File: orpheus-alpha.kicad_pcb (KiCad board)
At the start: 2 copper layers, 84.8 x 54.4 mm, 60 parts, among them J1 Signal in, J2 AC in, J3 Signal out, J4 uC

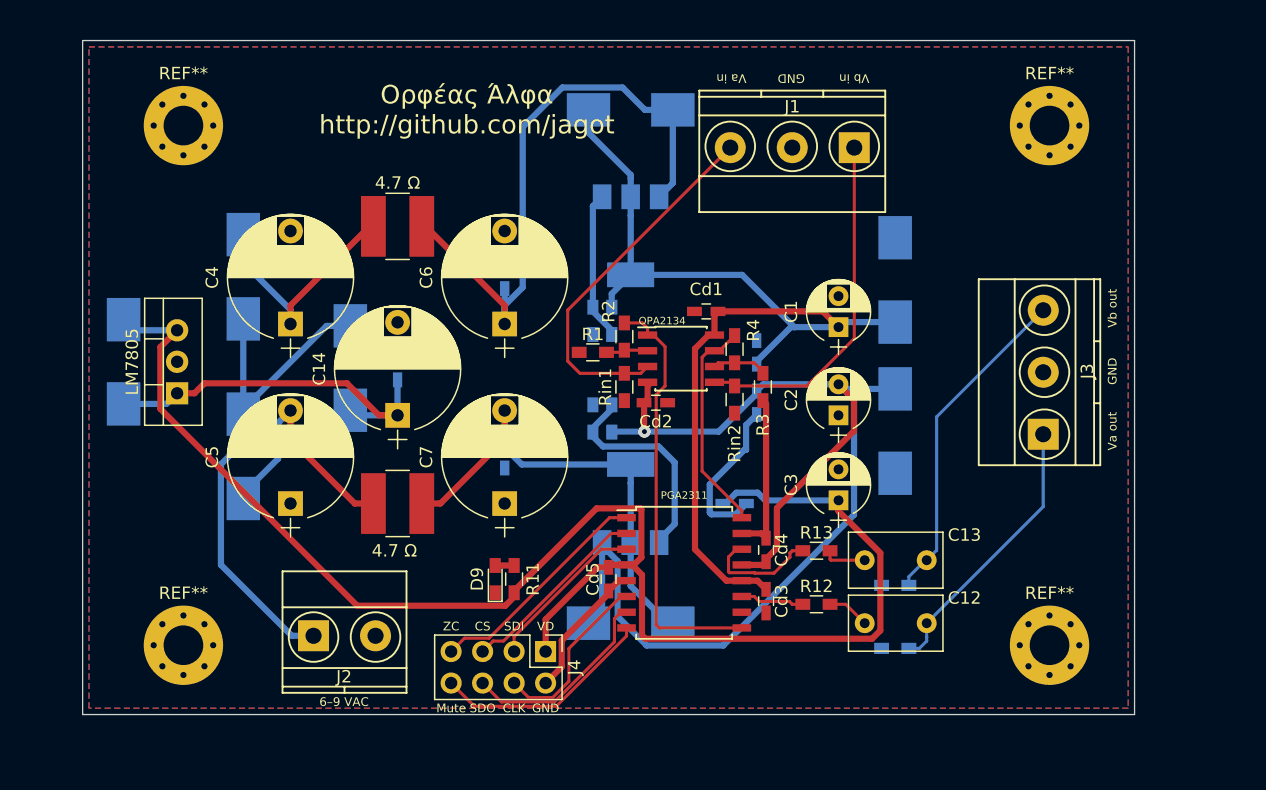
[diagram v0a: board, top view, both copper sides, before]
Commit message: Small changes, changed output coupling caps to film type
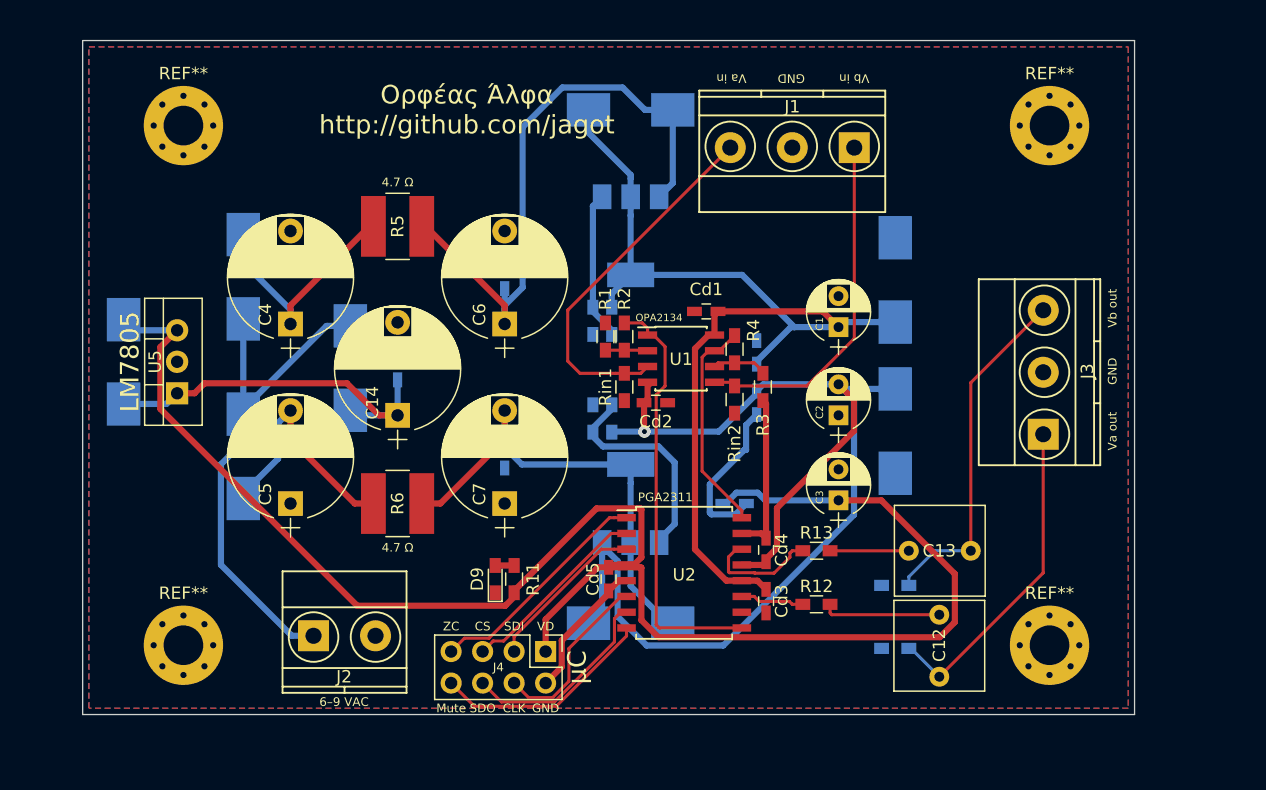
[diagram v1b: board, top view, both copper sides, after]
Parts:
- removed 4.7 Ω: 4.7, Resistors_SMD:R_1218_HandSoldering (x2)
- removed LM317: LM317_3PinPackage, TO_SOT_Packages_SMD:SOT-223-3Lead_TabPin2
- removed LM337: LM337_SOT223, TO_SOT_Packages_SMD:SOT-223-3Lead_TabPin2
- removed LM7805: LM7805_TO220, TO_SOT_Packages_THT:TO-220_Vertical
- removed OPA2134: OPA2134, Housings_SOIC:SOIC-8_3.9x4.9mm_Pitch1.27mm
- removed PGA2311: PGA2311, Housings_SOIC:SOIC-16W_7.5x10.3mm_Pitch1.27mm
- added R5: 4.7, Resistors_SMD:R_1218_HandSoldering, F.Cu at (108.7, 93.2)
- added R6: 4.7, Resistors_SMD:R_1218_HandSoldering, F.Cu at (108.7, 115.6)
- added U1: OPA2134, Housings_SOIC:SOIC-8_3.9x4.9mm_Pitch1.27mm, F.Cu at (131.6, 103.9)
- added U2: PGA2311, Housings_SOIC:SOIC-16W_7.5x10.3mm_Pitch1.27mm, F.Cu at (131.8, 121.2)
- added U3: LM317_3PinPackage, TO_SOT_Packages_SMD:SOT-223-3Lead_TabPin2, B.Cu at (127.5, 94.0)
- added U4: LM337_SOT223, TO_SOT_Packages_SMD:SOT-223-3Lead_TabPin2, B.Cu at (127.5, 115.6)
- added U5: LM7805_TO220, TO_SOT_Packages_THT:TO-220_Vertical, F.Cu at (90.9, 106.7)
- C12, C13: footprint Capacitors_THT:C_Disc_D7.5mm_W4.4mm_P5.00mm -> Capacitors_THT:C_Rect_L7.2mm_W7.2mm_P5.00mm_FKS2_FKP2_MKS2_MKP2
- moved C12 4.44 mm to (152.4, 129.5), turned to 90 degrees
- moved C13 3.64 mm to (154.9, 119.4)
- moved R1 1.63 mm to (125.5, 102.1), turned to 270 degrees
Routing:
- net VD: track 125.2 -> 136.7 mm
- net Net-(C12-Pad2): track 3.42 -> 9.56 mm
- net Va_out: track 22.3 -> 26.4 mm
- net Net-(C13-Pad2): track 3.52 -> 6.35 mm
- net Vb_out: track 26.7 -> 28.4 mm
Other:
- board text added: "4.7 Ω"
- board text added: "LM317"
- board text added: "LM337"
- board text added: "LM7805"
- board text added: "OPA2134"
- board text added: "PGA2311"
- board text added: "μC"

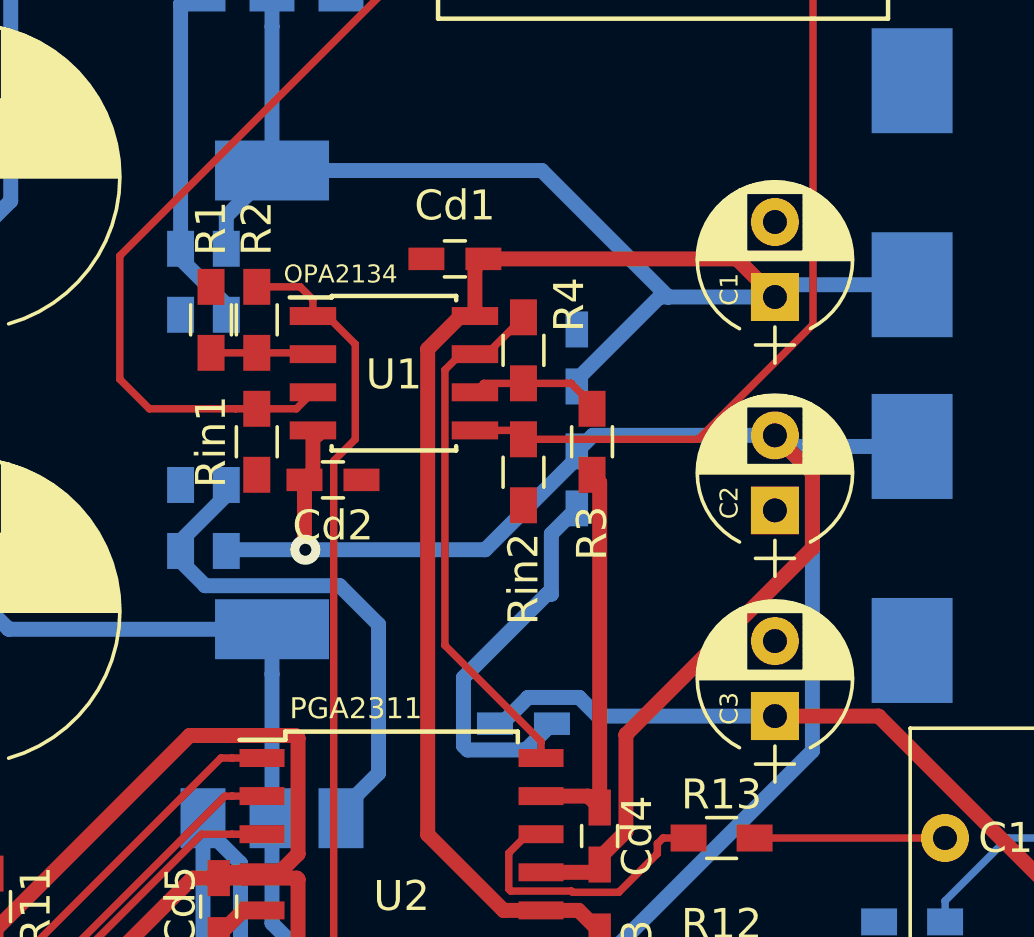
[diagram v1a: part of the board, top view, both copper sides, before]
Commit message: Added part numbers
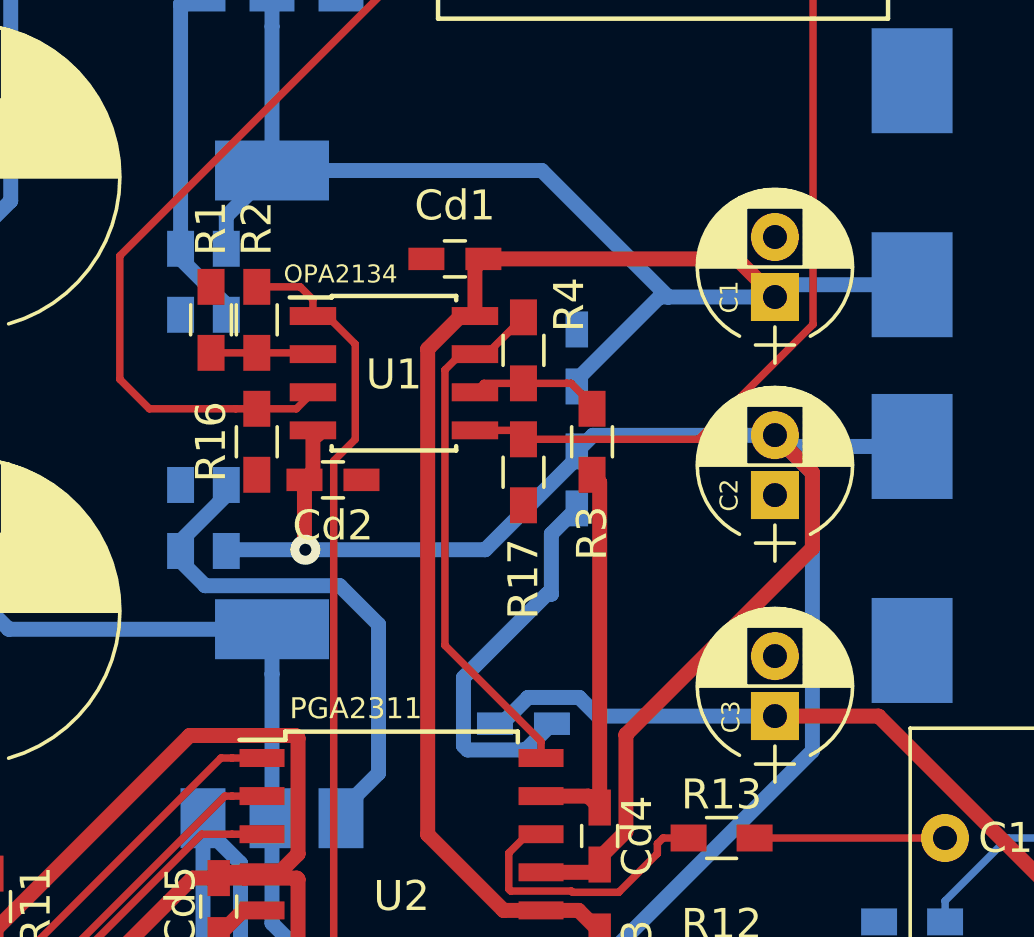
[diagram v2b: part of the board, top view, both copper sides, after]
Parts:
- C1, C2, C3: footprint Capacitors_THT:CP_Radial_D5.0mm_P2.50mm -> Capacitors_THT:CP_Radial_D5.0mm_P2.00mm
- moved C2 0.51 mm to (144.3, 108.0)
- renumbered Rin1 to R16, Rin2 to R17
